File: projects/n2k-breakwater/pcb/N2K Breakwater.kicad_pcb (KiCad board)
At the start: 4 copper layers, 68.2 x 43 mm, 52 parts, among them J1 Shield to Ground, J2 N2K, J3 Signals, J4 V_OUT, J5 GND, Q1 BSS126H6327XTSA2, Q2 SQJ872EP-T1_BE3, Q3 SQJ872EP-T1_BE3, Q4 BSS123NH6327XTSA1

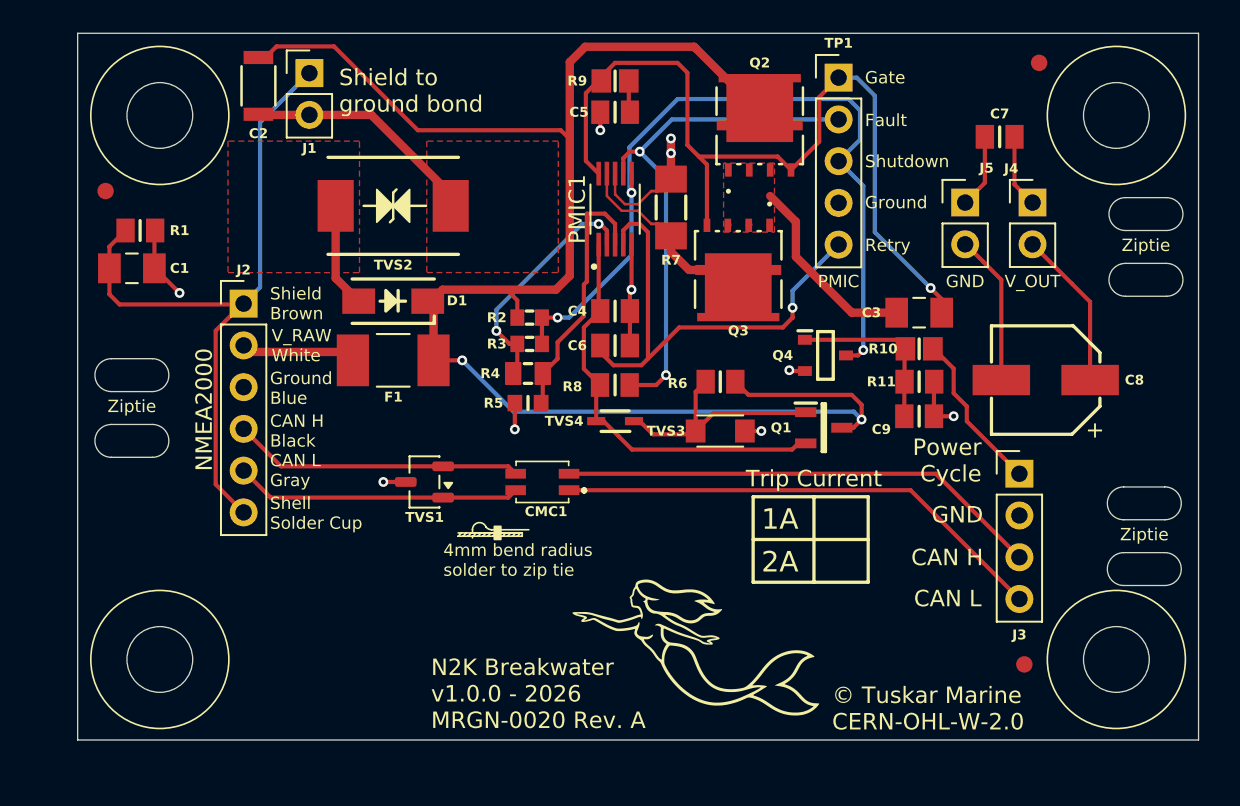
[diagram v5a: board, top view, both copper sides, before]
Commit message: Reworked the PCB and F1+R7 values.
Signed-off-by: digimer <digital.mermaid@gmail.com>
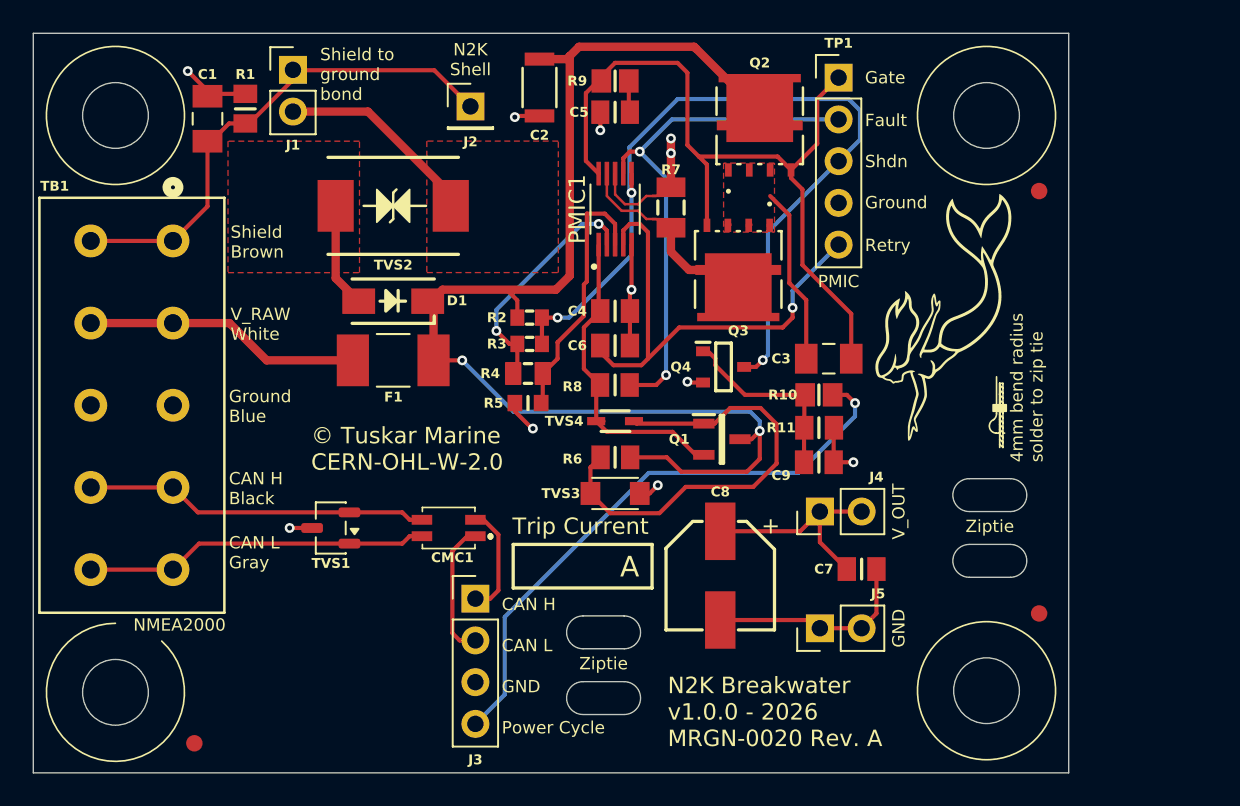
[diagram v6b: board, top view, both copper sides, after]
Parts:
- removed ZT5, ZT6: ~, mr-stuff:Tuskar Ziptie Slot 4.5x2mm
- added TB1: 1862440, mr-stuff:Phoenix Contact 1862440, F.Cu at (63.3, 107.6)
- F1: value 1A -> 2.5A
- J2: value N2K -> Shell; footprint Connector_PinHeader_2.54mm:PinHeader_1x06_P2.54mm_Vertical -> Connector_PinHeader_2.54mm:PinHeader_1x01_P2.54mm_Vertical
- R7: value 0.05R -> 0.033R; footprint mr-stuff:Vishay WSLP 1206 4-wire Kelvin -> mr-stuff:Vishay RCWE 1206 4-wire Kelvin
- moved FID3 34.0 mm to (69.6, 118.2)
- moved J3 34.0 mm to (86.7, 109.4)
- moved ZT3 33.8 mm to (94.5, 111.5)
- moved ZT4 33.8 mm to (94.5, 115.5)
- moved C7 27.6 mm to (110.2, 107.6), turned to 0 degrees
- moved J5 27.4 mm to (107.7, 111.2), turned to 90 degrees
- moved REF** 24.2 mm to (103.7, 110.8), turned to 90 degrees
- moved C8 23.1 mm to (101.6, 108.0), turned to -90 degrees
- moved J4 22.8 mm to (107.7, 104.1), turned to 90 degrees
- moved ZT1 19.6 mm to (118.0, 103.1)
- moved ZT2 19.6 mm to (118.0, 107.1)
- moved J2 18.3 mm to (86.4, 79.5)
- moved C2 17.1 mm to (90.6, 78.3)
- moved C1 10.2 mm to (70.4, 80.2), turned to -90 degrees
- moved R1 9.78 mm to (72.7, 79.6), turned to -90 degrees
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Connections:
- J3 pad 1: /POWER_CYCLE -> /SAFE_CAN_H
- J3 pad 2: GND -> /SAFE_CAN_L
- J3 pad 3: /SAFE_CAN_H -> GND
- J3 pad 4: /SAFE_CAN_L -> /POWER_CYCLE
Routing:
- net /POWER_CYCLE: track 9.82 -> 36.0 mm, vias 0 -> 1
- net V_RAW: track 102.0 -> 77.6 mm
- net /SAFE_CAN_H: track 29.5 -> 6.78 mm
- net /SAFE_CAN_L: track 30.1 -> 8.36 mm
- net Net-(Q1-G): track 14.5 -> 27.5 mm
- net Net-(J1-Pin_1): track 42.5 -> 31.0 mm
- net /M12_V_RAW: track 7.02 -> 16.9 mm
- net /PMIC_VIN: track 25.3 -> 19.5 mm
- net /PMIC_GATE: track 52.7 -> 48.2 mm, vias 1 -> 0
- net /M12_CAN_L: track 17.4 -> 21.0 mm
- net /M12_CAN_H: track 17.8 -> 21.0 mm
- net /PMIC_SHDN: track 48.9 -> 50.9 mm
- net Net-(Q4-G): track 10.5 -> 11.7 mm
- net V_OUT: track 16.9 -> 15.8 mm
- net Net-(C3-Pad1): track 12.0 -> 11.0 mm
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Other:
- board size 68.2 x 43 mm -> 63 x 45 mm
- board text added: "A"
- board text added: "N2K Shell"
- board text added: "Shdn"
- board text removed: "1A"
- board text removed: "2A"
- board text removed: "Shell Solder Cup"
- board text removed: "Shutdown"
